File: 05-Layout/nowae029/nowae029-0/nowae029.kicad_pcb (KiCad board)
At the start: 2 copper layers, 100 x 99.9 mm, 175 parts, among them P101 COMM_3, P102 SUPPLY_3, P103 COMM_4, P104 SUPPLY_4, P201 DEBUG, P401 BATTERY, P501 632722110112, U201 STM32L073CBT6, U301 TCA9554PWR, U302 TCA9554PWR, U401 TLV70233DBV, U501 FT230XS, U601 TCA9554PWR, U602 TCA9554PWR, Y201 32768

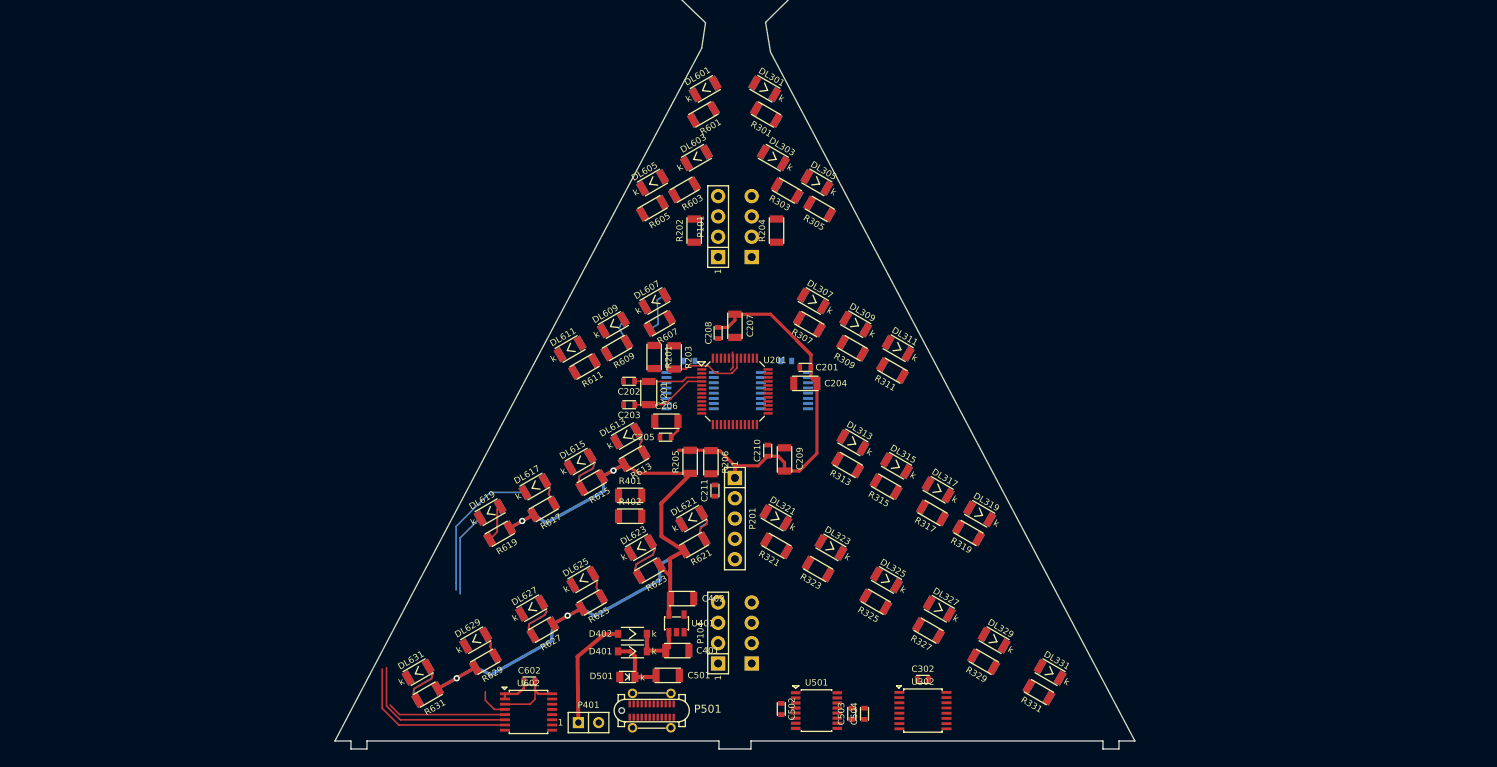
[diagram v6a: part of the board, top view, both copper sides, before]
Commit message: WiP: PCB removed some LEDs and placed in other way the others
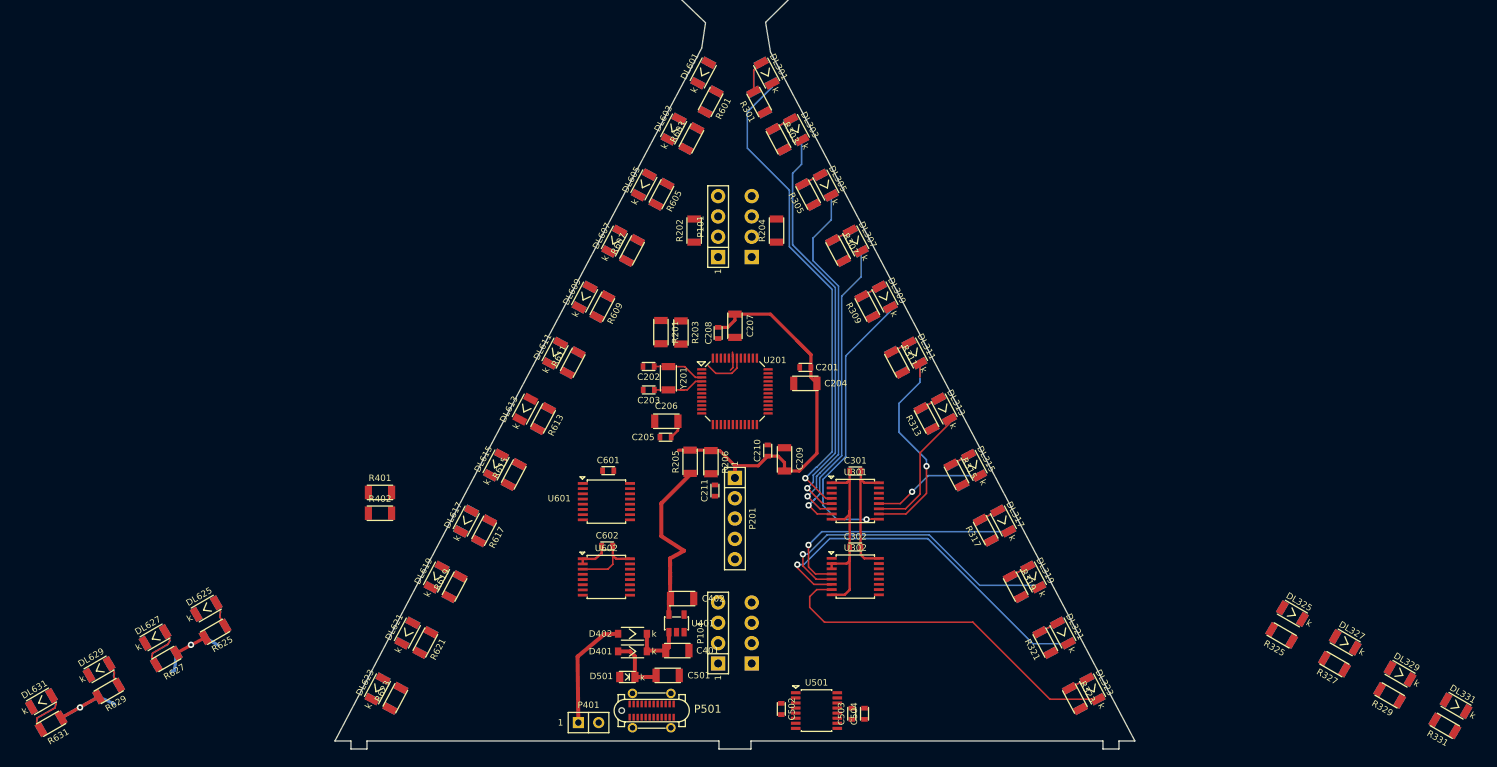
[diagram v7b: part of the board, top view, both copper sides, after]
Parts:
- C301, C601, U301, U601: moved to F.Cu
- moved DL327 50.9 mm to (176.3, 136.7)
- moved DL328 50.9 mm to (176.3, 136.7)
- moved R325 50.9 mm to (168.3, 135.8)
- moved R326 50.9 mm to (168.3, 135.8)
- moved R329 50.9 mm to (181.8, 143.3)
- moved R330 50.9 mm to (181.8, 143.3)
- moved R331 50.9 mm to (188.7, 147.1)
- moved R332 50.9 mm to (188.7, 147.1)
- moved R327 50.9 mm to (174.9, 139.4)
- moved R328 50.9 mm to (174.9, 139.4)
- moved DL325 50.9 mm to (169.7, 133.1)
- moved DL326 50.9 mm to (169.7, 133.1)
- moved DL329 50.9 mm to (183.1, 140.6)
- moved DL330 50.9 mm to (183.1, 140.6)
- moved DL331 50.9 mm to (190.1, 144.6)
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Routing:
- net /Branch1/B1_LINE1: track 0.00 -> 60.8 mm, vias 0 -> 1
- net /Branch1/B1_LINE2: track 0.00 -> 51.5 mm, vias 0 -> 1
- net +3.3V: track 116.3 -> 68.9 mm, vias 4 -> 2
- net /Branch1/B1_LINE11: track 0.00 -> 46.3 mm, vias 0 -> 1
- net /Branch1/B1_LINE3: track 0.00 -> 45.7 mm, vias 0 -> 1
- net /Branch1/B1_LINE12: track 0.00 -> 45.2 mm
- net /Branch1/B1_LINE10: track 0.00 -> 38.9 mm, vias 0 -> 1
- net /Branch1/B1_LINE4: track 0.00 -> 38.9 mm, vias 0 -> 1
- net /Branch1/B1_LINE5: track 0.00 -> 36.9 mm, vias 0 -> 1
- net /Branch1/B1_LINE9: track 0.00 -> 31.8 mm, vias 0 -> 1
- net /Branch1/B1_LINE6: track 0.00 -> 27.5 mm, vias 0 -> 1
- net GND: track 6.62 -> 32.6 mm
- net /Branch2/B2_LINE10: track 25.4 -> 0.00 mm
- net /Branch2/B2_LINE9: track 22.3 -> 0.00 mm
- net /Branch2/B2_LINE12: track 21.1 -> 0.00 mm
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
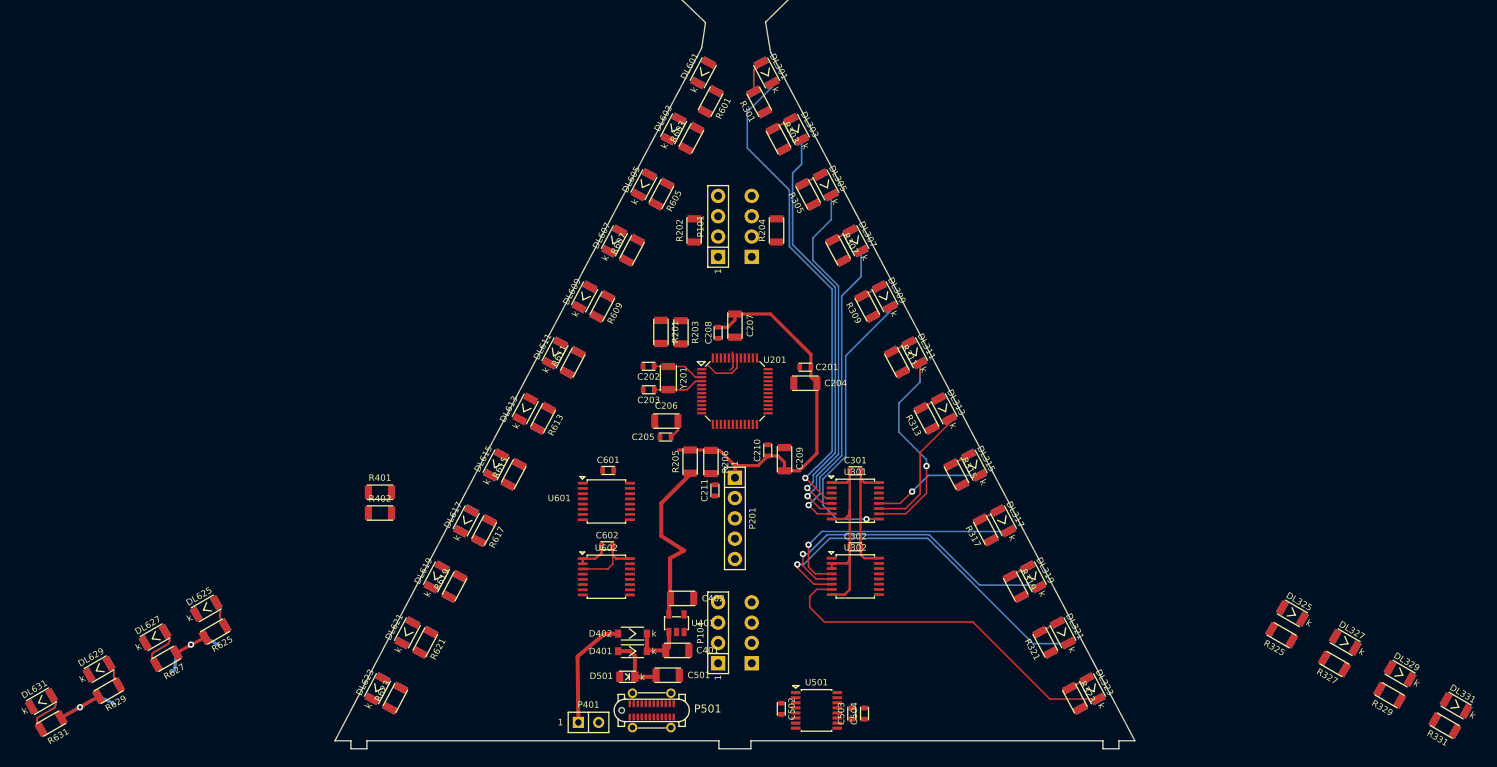
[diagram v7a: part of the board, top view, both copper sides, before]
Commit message: Removed LEDs, added star page, WiP PCB
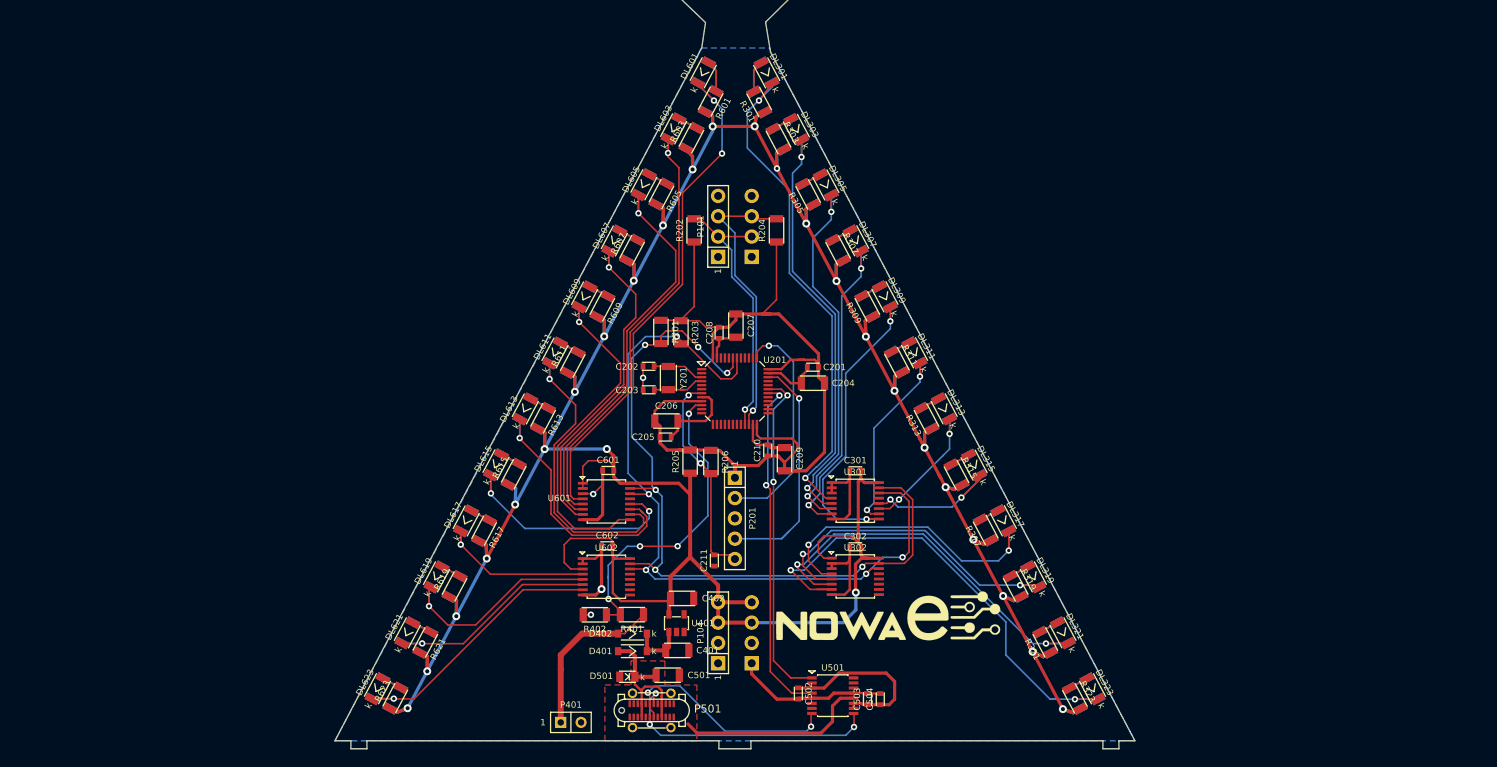
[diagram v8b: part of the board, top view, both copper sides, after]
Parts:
- removed DL325, DL326, DL327, DL328, DL329, DL330, DL331, DL332, DL625, DL626, DL627, DL628, DL629, DL630, DL631, DL632: MISC, LEDs:LED-1206
- removed R325, R326, R327, R328, R329, R330, R331, R332, R625, R626, R627, R628, R629, R630, R631, R632: 270, RESISTOR:RESISTOR-1206
- added G***: LOGO, LOGO:LOGO_NOWAE_30MM_FSILK, F.Cu at (119.2, 133.4)
- moved R401 35.0 mm to (87.1, 133.2), turned to 180 degrees
- moved R402 29.7 mm to (82.5, 133.2), turned to 180 degrees
- moved C211 8.76 mm to (97.4, 126.5)
- moved DL616 7.95 mm to (70.2, 114.5)
- moved DL614 7.90 mm to (73.8, 107.5)
- moved C502 2.86 mm to (107.9, 143.1)
- moved U501 2.74 mm to (112.2, 143.4)
- moved C503 2.68 mm to (116.6, 143.8)
- moved C504 2.68 mm to (118.2, 143.8)
- moved P401 2.20 mm to (79.5, 146.7)
- moved C201 0.95 mm to (109.8, 102.3)
- moved C204 0.95 mm to (109.8, 104.3)
- moved C207 0.12 mm to (100.1, 97.1)
- moved C208 0.12 mm to (98.0, 98.0)
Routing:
- net +3.3V: track 68.9 -> 447.5 mm, vias 2 -> 26
- net /Branch1/BRANCH1_SDA: track 2.40 -> 99.5 mm, vias 0 -> 6
- net /Branch1/BRANCH1_SCL: track 5.50 -> 99.9 mm, vias 0 -> 5
- net /Microcontroller/VDD_MCU: track 53.8 -> 119.8 mm
- net GND: track 32.6 -> 98.4 mm, vias 0 -> 4
- net /Branch2/B2_LINE1: track 0.00 -> 65.4 mm, vias 0 -> 2
- net /Branch2/B2_LINE2: track 0.00 -> 55.7 mm, vias 0 -> 1
- net /Branch2/B2_LINE3: track 0.00 -> 50.9 mm, vias 0 -> 1
- net /Communication/COMM_RX: track 0.00 -> 43.8 mm, vias 0 -> 2
- net /Branch2/B2_LINE5: track 0.00 -> 43.3 mm, vias 0 -> 1
- net /Communication/COMM_TX: track 0.00 -> 42.3 mm, vias 0 -> 2
- net /Branch2/B2_LINE4: track 0.00 -> 41.9 mm, vias 0 -> 1
- net /Power Supply/BATTERY_STATUS: track 0.00 -> 39.8 mm, vias 0 -> 4
- net /Branch2/B2_LINE6: track 0.00 -> 38.4 mm, vias 0 -> 1
- net +VUSB: track 7.68 -> 44.4 mm
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- added copper zone on F.Cu, net +VUSB
- added copper zone on B.Cu, net GND
